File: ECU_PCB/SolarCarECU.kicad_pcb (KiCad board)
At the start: 4 copper layers, 160 x 100 mm, 121 parts, among them J1 Screw_Terminal_01x02, J2 USB_B_Micro, J3 Screw_Terminal_01x05, J4 Screw_Terminal_01x08, J5 Screw_Terminal_01x08, J6 Screw_Terminal_01x14, J7 Screw_Terminal_01x14, Q1 QM6015D, Q2 PZT2222A, Q3 QM6015D, Q4 QM6015D, Q5 QM6015D, Q6 QM6015D, U1 Teensy3.6, U10 LM324A, U2 EL7202CN, U3 EL7202CN, U4 L7805, U5 MCP2562-E-P, U6 MCP2562-E-P, U7 4504, U8 4504, U9 4504

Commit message: PCB prototype finished, documention added
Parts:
- added BT1: Battery_Cell, Battery:BatteryHolder_Keystone_1060_1x2032, F.Cu at (141.2, 65.5)
- added R52: 1k, Resistor_SMD:R_0603_1608Metric, F.Cu at (222.8, 96.3)
- added R53: 1k, Resistor_SMD:R_0603_1608Metric, F.Cu at (222.8, 98.0)
- added R54: 47, Resistor_SMD:R_0603_1608Metric, F.Cu at (237.5, 118.1)
- added R55: 47, Resistor_SMD:R_0603_1608Metric, F.Cu at (237.5, 115.6)
- added R56: 47, Resistor_SMD:R_0603_1608Metric, F.Cu at (237.5, 113.0)
- added R57: 47, Resistor_SMD:R_0603_1608Metric, F.Cu at (237.5, 110.5)
- J2: value USB_B_Micro -> USB_B; footprint SamacSys_Parts:USBRBSSOTH -> Connector_USB:USB_B_OST_USB-B1HSxx_Horizontal
- R42, R5: value 0 -> 47
- R43: footprint Resistor_SMD:R_0603_1608Metric -> Resistor_SMD:R_1206_3216Metric
- moved R42 90.2 mm to (237.5, 120.7)
- moved R5 38.1 mm to (237.5, 123.2)
- moved R43 35.8 mm to (114.6, 133.9), turned to 90 degrees
- moved R46 32.3 mm to (95.2, 119.3)
- moved R47 32.3 mm to (98.4, 119.3)
- moved C19 12.9 mm to (225.9, 60.5), turned to 0 degrees
- moved R44 10.2 mm to (96.0, 94.6)
- moved R45 10.2 mm to (99.2, 94.6)
- moved C15 6.86 mm to (225.9, 50.3), turned to 180 degrees
- moved R11 5.72 mm to (232.4, 136.9)
- moved R9 5.61 mm to (231.9, 121.2)
- moved C11 4.58 mm to (219.6, 136.3)
- moved C12 4.58 mm to (219.5, 124.7)
- moved R1 4.58 mm to (218.3, 131.2)
- moved R2 4.58 mm to (218.3, 138.8)
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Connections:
- net Net-(U1-Pad23) renamed /UART_4_RX
- net Net-(U1-Pad24) renamed /UART_4_TX
- J2 pad 4: Net-(J2-Pad4) -> GND
- J4 pad 2: /MOTOR_L_THROTTLE -> /MOTOR_R_THROTTLE
- J4 pad 3: /MOTOR_L_REGEN -> /MOTOR_R_METER
- J4 pad 4: /MOTOR_L_FWD_EN -> /MOTOR_R_REGEN_EN
- J4 pad 5: /MOTOR_L_REV_EN -> /MOTOR_R_ECO_EN
- J4 pad 6: /MOTOR_L_METER -> /MOTOR_R_FWD_EN
- J4 pad 7: /MOTOR_R_METER -> /MOTOR_R_REV_EN
- J5 pad 1: /MOTOR_R_ECO_EN -> /MOTOR_L_REGEN
- J5 pad 2: /MOTOR_R_REGEN_EN -> /MOTOR_L_THROTTLE
- J5 pad 3: /MOTOR_R_FWD_EN -> /MOTOR_L_METER
- J5 pad 6: /MOTOR_R_REV_EN -> /MOTOR_L_FWD_EN
- J5 pad 7: /MOTOR_R_THROTTLE -> /MOTOR_L_REV_EN
- J7 pad 1: +12V -> +5V
- J7 pad 10: /CS_0 -> Net-(J7-Pad10)
- J7 pad 11: /MISO_0 -> Net-(J7-Pad11)
- J7 pad 12: /MOSI_0 -> Net-(J7-Pad12)
- J7 pad 13: /SCK_0 -> Net-(J7-Pad13)
- J7 pad 6: +5V -> /SCL_0
- J7 pad 7: /UART_RX -> /SDA_0
- J7 pad 8: /UART_TX -> Net-(J7-Pad8)
- J7 pad 9: GND -> Net-(J7-Pad9)
- R42 pad 1: +12V -> Net-(J7-Pad9)
- R42 pad 2: Net-(C1-Pad1) -> /UART_1_TX
- R5 pad 1: Net-(J2-Pad4) -> Net-(J7-Pad8)
- R5 pad 2: /USB_MASTER-SLAVE_SEL -> /UART_1_RX
- U1 pad 10: Net-(U1-Pad10) -> /UART_3_TX
- U1 pad 76: Net-(U1-Pad76) -> /UART_6_RX
- U1 pad 77: Net-(U1-Pad77) -> /UART_6_TX
- U1 pad 84: /LV_HEADLIGHTS -> /LV_HORN
- U1 pad 85: /LV_HORN -> /LV_HEADLIGHTS
- U1 pad 9: Net-(U1-Pad9) -> /UART_3_RX
- U8 pad 10: /MOTOR_R_FWD_EN -> /MOTOR_L_REGEN_EN
- U8 pad 11: /LV_MOTOR_R_REGEN_EN -> GND
- U8 pad 12: /MOTOR_R_REGEN_EN -> Net-(U8-Pad12)
- U8 pad 14: /LV_MOTOR_R_ECO_EN -> GND
- U8 pad 15: /MOTOR_R_ECO_EN -> Net-(U8-Pad15)
- U8 pad 2: /MOTOR_L_REGEN_EN -> /MOTOR_L_REV_EN
- U8 pad 3: /LV_MOTOR_L_REGEN_EN -> /LV_MOTOR_L_REV_EN
- U8 pad 4: /MOTOR_L_ECO_EN -> /MOTOR_L_FWD_EN
- U8 pad 5: /LV_MOTOR_L_ECO_EN -> /LV_MOTOR_L_FWD_EN
- U8 pad 6: /MOTOR_R_REV_EN -> /MOTOR_L_ECO_EN
- U8 pad 7: /LV_MOTOR_R_REV_EN -> /LV_MOTOR_L_ECO_EN
- U8 pad 9: /LV_MOTOR_R_FWD_EN -> /LV_MOTOR_L_REGEN_EN
- U9 pad 10: /HAZARD_LED -> /MOTOR_R_REGEN_EN
- U9 pad 11: /LV_MOTOR_L_REV_EN -> /LV_MOTOR_R_ECO_EN
- U9 pad 12: /MOTOR_L_REV_EN -> /MOTOR_R_ECO_EN
- U9 pad 14: /LV_MOTOR_L_FWD_EN -> GND
- U9 pad 15: /MOTOR_L_FWD_EN -> Net-(U9-Pad15)
- U9 pad 2: Net-(U9-Pad2) -> /HAZARD_LED
- U9 pad 3: GND -> /LV_HAZARD_LED
- U9 pad 4: Net-(U9-Pad4) -> /MOTOR_R_REV_EN
- U9 pad 5: GND -> /LV_MOTOR_R_REV_EN
- U9 pad 6: Net-(U9-Pad6) -> /MOTOR_R_FWD_EN
- U9 pad 7: GND -> /LV_MOTOR_R_FWD_EN
- U9 pad 9: /LV_HAZARD_LED -> /LV_MOTOR_R_REGEN_EN
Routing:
- net +12V: track 24.5 -> 411.4 mm, vias 2 -> 12
- net +5V: track 41.4 -> 287.3 mm, vias 1 -> 4
- net /HAZARD_LED: track 0.00 -> 168.2 mm, vias 0 -> 2
- net GNDA: track 323.4 -> 207.6 mm, vias 17 -> 16
- net /LV_SEL_CTRL: track 0.00 -> 96.0 mm, vias 0 -> 1
- net /LV_UP_CTRL: track 0.00 -> 93.0 mm, vias 0 -> 1
- net /LV_GEARSHIFT_CTRL: track 3.02 -> 94.9 mm, vias 0 -> 1
- net /LV_THROTTLE_CTRL: track 3.02 -> 94.5 mm, vias 0 -> 1
- net /LV_TURNSIG_CTRL: track 3.02 -> 94.5 mm, vias 0 -> 1
- net /UART_6_RX: track 0.00 -> 90.1 mm, vias 0 -> 1
- net /UART_6_TX: track 0.00 -> 87.6 mm, vias 0 -> 1
- net /LV_DOWN_CTRL: track 0.00 -> 86.9 mm, vias 0 -> 1
- net /LV_BLINKERS: track 0.00 -> 85.3 mm, vias 0 -> 1
- net /LV_HAZARD_CTRL: track 0.00 -> 80.0 mm, vias 0 -> 1
- net /LV_HAZARD_LED: track 0.00 -> 79.8 mm
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- added copper zone on F.Cu, net +12V

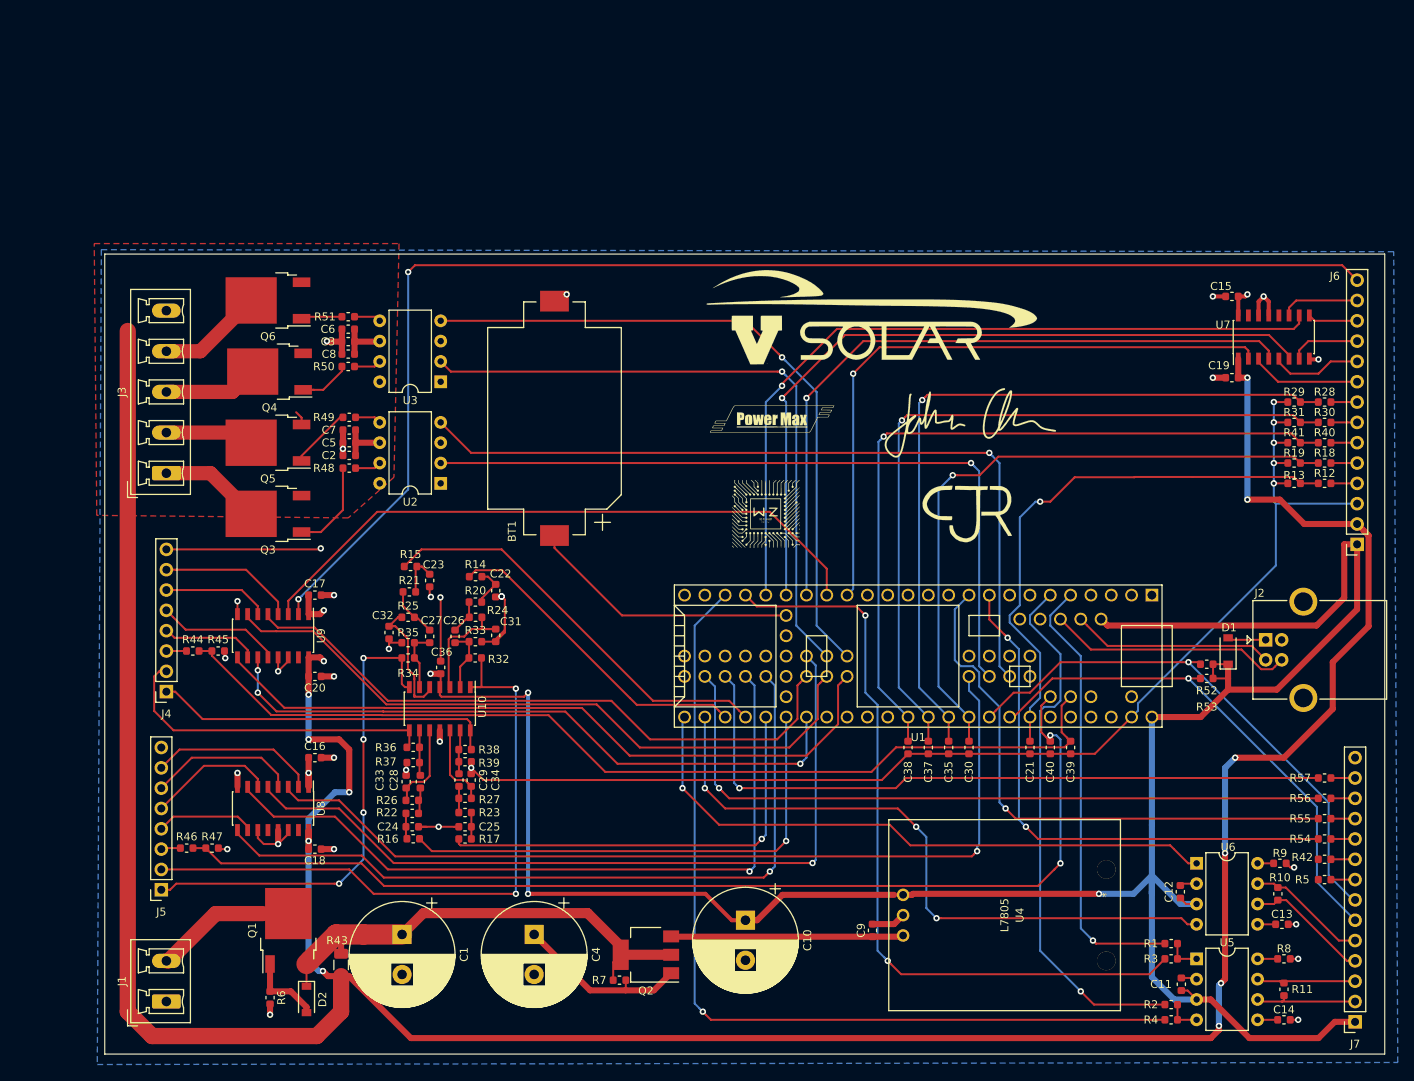
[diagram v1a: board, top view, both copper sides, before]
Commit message: fixed UART_1_* pins, added LV_KILL_SENSE, added *STEER_CTRL*
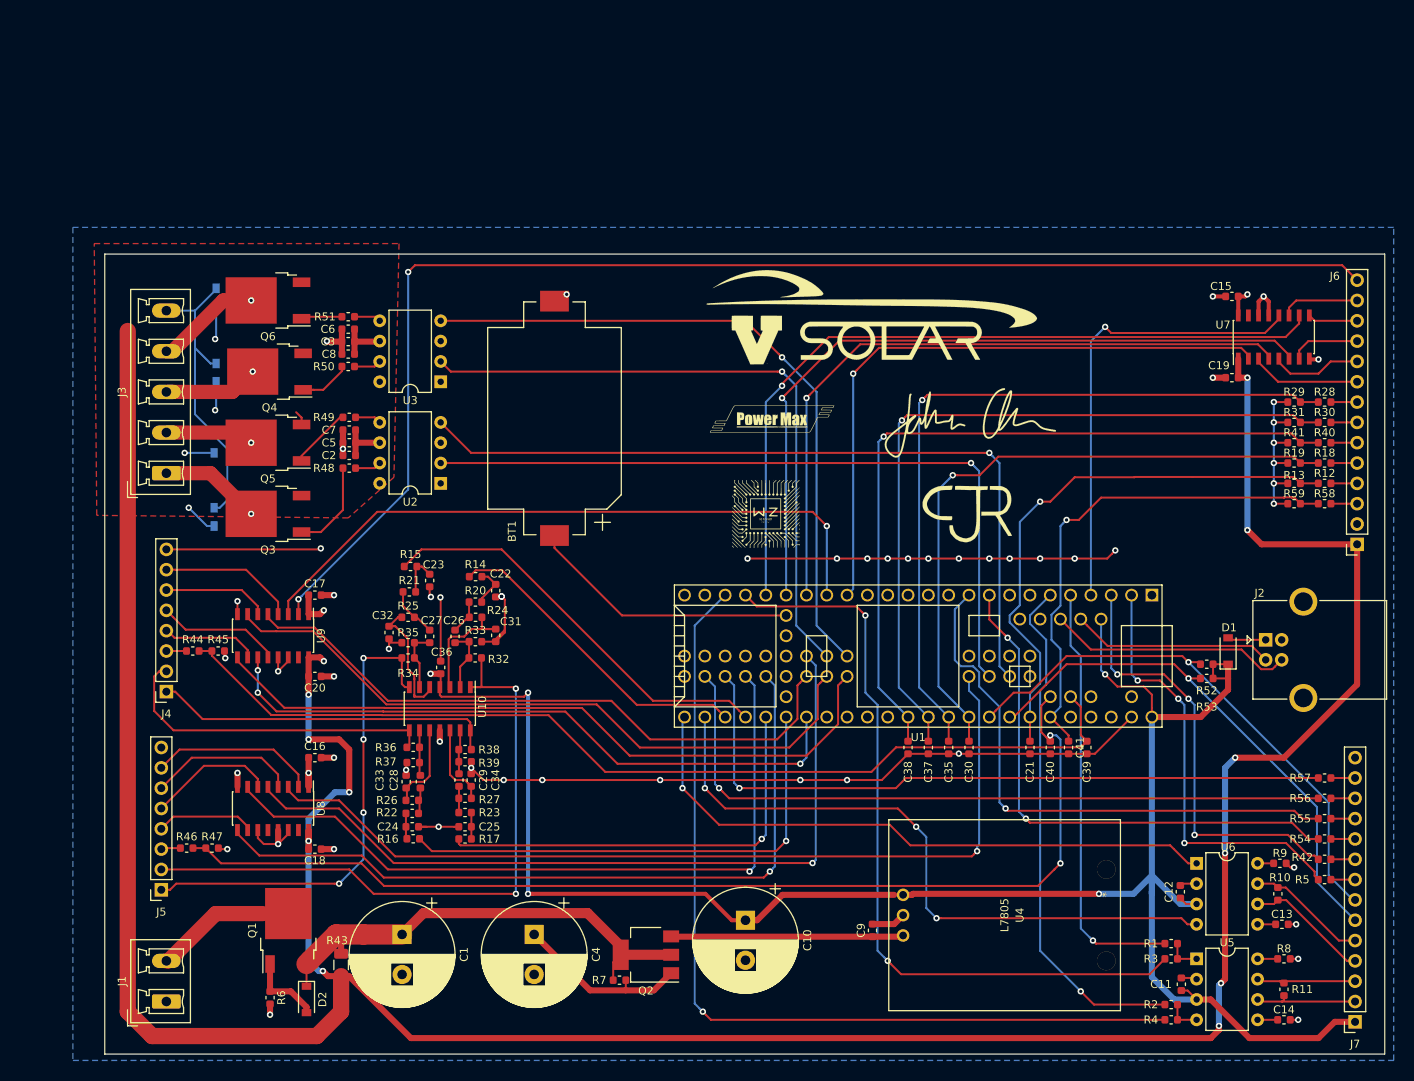
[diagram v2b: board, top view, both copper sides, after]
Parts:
- added C41: C, Capacitor_SMD:C_0603_1608Metric, F.Cu at (205.5, 106.7)
- added D10: D, Diode_SMD:D_SOD-123, B.Cu at (100.6, 49.3)
- added D3: D, Diode_SMD:D_SOD-123, B.Cu at (100.3, 79.0)
- added D4: D, Diode_SMD:D_SOD-123, B.Cu at (100.3, 76.7)
- added D5: D, Diode_SMD:D_SOD-123, B.Cu at (100.6, 61.0)
- added D6: D, Diode_SMD:D_SOD-123, B.Cu at (100.6, 58.7)
- added D7: D, Diode_SMD:D_SOD-123, B.Cu at (100.3, 69.8)
- added D8: D, Diode_SMD:D_SOD-123, B.Cu at (100.3, 67.6)
- added D9: D, Diode_SMD:D_SOD-123, B.Cu at (100.6, 51.8)
- added R58: R, Resistor_SMD:R_0603_1608Metric, F.Cu at (237.5, 76.2)
- added R59: R, Resistor_SMD:R_0603_1608Metric, F.Cu at (233.7, 76.2)
- moved C39 2.03 mm to (207.8, 106.7)
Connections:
- J6 pad 1: +5V -> +12V
- J6 pad 2: +12V -> GNDA
- J6 pad 3: GNDA -> /STEER_CTRL
- U1 pad 2: /UART_RX -> /UART_1_RX
- U1 pad 3: /UART_TX -> /UART_1_TX
- U1 pad 4: Net-(U1-Pad4) -> /LV_KILL_SENSE
- U1 pad 48: Net-(U1-Pad48) -> /LV_STEER_CTRL
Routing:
- net /LV_STEER_CTRL: track 0.00 -> 63.4 mm, vias 0 -> 1
- net /LV_KILL_SENSE: track 0.00 -> 57.5 mm, vias 0 -> 1
- net /UART_1_TX: track 0.00 -> 54.4 mm, vias 0 -> 3
- net /UART_1_RX: track 0.00 -> 54.3 mm, vias 0 -> 3
- net +5V: track 287.3 -> 235.2 mm, vias 4 -> 5
- net GND: track 55.4 -> 93.8 mm
- net +12V: track 411.4 -> 426.2 mm, vias 12 -> 16
- net GNDA: track 207.6 -> 211.5 mm, vias 16 -> 35
- net /HORN: track 12.7 -> 16.4 mm, vias 0 -> 1
- net /HEADLIGHTS: track 11.1 -> 14.7 mm, vias 0 -> 1
- net /BRAKELIGHTS: track 11.8 -> 15.3 mm, vias 0 -> 1
- net /BLINKERS: track 13.2 -> 16.7 mm, vias 0 -> 1
- net /STEER_CTRL: track 0.00 -> 3.28 mm
- net /LV_HAZARD_LED: track 79.8 -> 83.0 mm, vias 0 -> 1
- net Net-(R2-Pad2): track 67.3 -> 65.0 mm
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
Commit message: reworked PCB and fixed all issues brought up
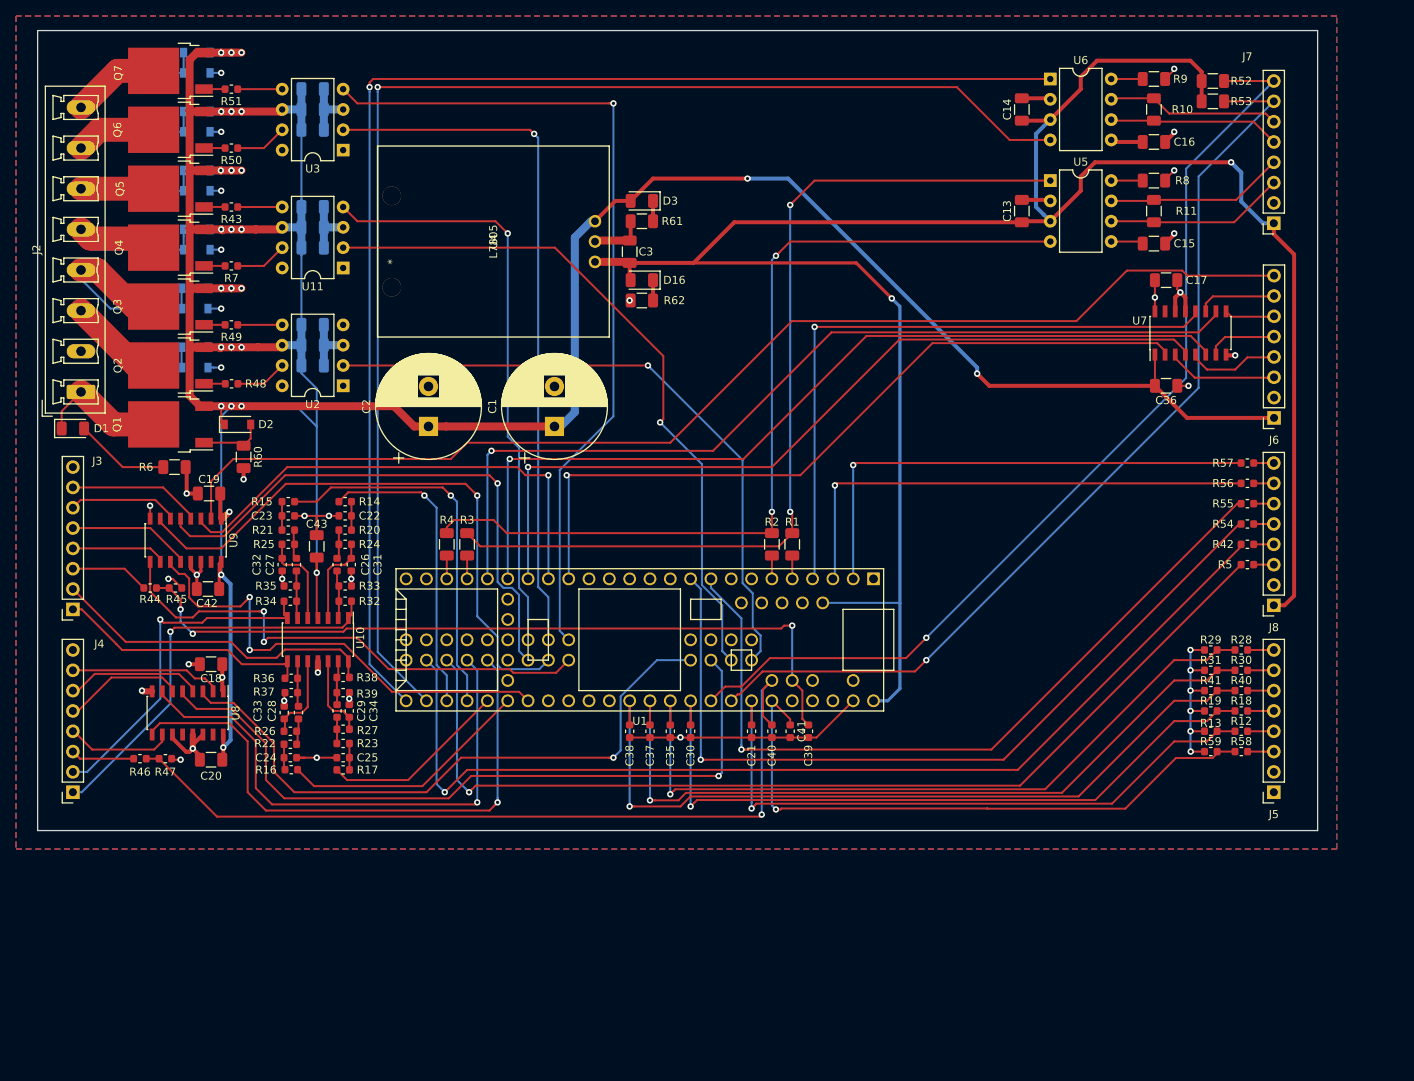
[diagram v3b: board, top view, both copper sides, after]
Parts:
- removed BT1: Battery_Cell, Battery:BatteryHolder_Keystone_1060_1x2032
- removed J1: Screw_Terminal_01x02, Connector_Phoenix_MC_HighVoltage:PhoenixContact_MCV_1,5_2-G-5.08_1x02_P5.08mm_Vertical
- added C42: 4.7u, Capacitor_SMD:C_1206_3216Metric, F.Cu at (97.9, 86.9)
- added C43: 100n, Capacitor_SMD:C_1206_3216Metric, F.Cu at (111.5, 81.5)
- added D11: D, Diode_SMD:D_SOD-123, B.Cu at (96.3, 51.8)
- added D12: D, Diode_SMD:D_SOD-123, B.Cu at (96.5, 34.5)
- added D13: D, Diode_SMD:D_SOD-123, B.Cu at (96.5, 37.1)
- added D14: D, Diode_SMD:D_SOD-123, B.Cu at (96.5, 19.8)
- added D15: D, Diode_SMD:D_SOD-123, B.Cu at (96.5, 22.4)
- added D16: 599-0291, LED_SMD:LED_1206_3216Metric, F.Cu at (152.1, 48.3)
- added J8: Screw_Terminal_01x08, Connector_PinSocket_2.54mm:PinSocket_1x08_P2.54mm_Vertical, F.Cu at (231.1, 88.9)
- added Q7: QM6015D, Package_TO_SOT_SMD:TO-252-2, F.Cu at (93.2, 22.1)
- added R60: 1k, Resistor_SMD:R_1206_3216Metric, F.Cu at (102.4, 70.4)
- added R61: 1k, Resistor_SMD:R_1206_3216Metric, F.Cu at (152.1, 40.9)
- added R62: 1k, Resistor_SMD:R_1206_3216Metric, F.Cu at (152.1, 50.8)
- added U11: MCP1403, Package_DIP:DIP-8_W7.62mm, F.Cu at (114.8, 46.7)
- C10: value 10uF -> 100n; footprint Capacitor_THT:CP_Radial_D13.0mm_P5.00mm -> Capacitor_SMD:C_1206_3216Metric; moved to B.Cu
- C11: value 0.47u -> 4.7u; footprint Capacitor_SMD:C_0603_1608Metric -> Capacitor_SMD:C_1206_3216Metric; moved to B.Cu
- C12: value 0.47u -> 47u; footprint Capacitor_SMD:C_0603_1608Metric -> Capacitor_SMD:C_1206_3216Metric; moved to B.Cu
- C13, C14, C15, C16, C17: value 0.47u -> 100n; footprint Capacitor_SMD:C_0603_1608Metric -> Capacitor_SMD:C_1206_3216Metric
- C18, C19: value 4.7u -> 100n; footprint Capacitor_SMD:C_0603_1608Metric -> Capacitor_SMD:C_1206_3216Metric
- C2: value 0.47u -> 470uF; footprint Capacitor_SMD:C_0603_1608Metric -> Capacitor_THT:CP_Radial_D13.0mm_P5.00mm
- C20: footprint Capacitor_SMD:C_0603_1608Metric -> Capacitor_SMD:C_1206_3216Metric
- C21, C30, C35, C37, C38, C39, C40, C41: value C -> 1n
- C3: value 0.47u -> 10uF; footprint Capacitor_SMD:C_0603_1608Metric -> Capacitor_SMD:C_1206_3216Metric
- C36: value 0.47u -> 4.7u; footprint Capacitor_SMD:C_0603_1608Metric -> Capacitor_SMD:C_1206_3216Metric
- C4: value 470uF -> 100n; footprint Capacitor_THT:CP_Radial_D13.0mm_P5.00mm -> Capacitor_SMD:C_1206_3216Metric; moved to B.Cu
- C5: footprint Capacitor_SMD:C_0603_1608Metric -> Capacitor_SMD:C_1206_3216Metric; moved to B.Cu
- C6: value 4.7u -> 47u; footprint Capacitor_SMD:C_0603_1608Metric -> Capacitor_SMD:C_1206_3216Metric; moved to B.Cu
- C7: value 47u -> 100n; footprint Capacitor_SMD:C_0603_1608Metric -> Capacitor_SMD:C_1206_3216Metric; moved to B.Cu
- C8: value 47u -> 4.7u; footprint Capacitor_SMD:C_0603_1608Metric -> Capacitor_SMD:C_1206_3216Metric; moved to B.Cu
- C9: value 10uF -> 47u; footprint Capacitor_SMD:C_0603_1608Metric -> Capacitor_SMD:C_1206_3216Metric; moved to B.Cu
- D1: value D_Schottky -> 599-0210; footprint Diode_SMD:D_SOD-123 -> LED_SMD:LED_1206_3216Metric
- D3: value D -> 599-0230; footprint Diode_SMD:D_SOD-123 -> LED_SMD:LED_1206_3216Metric; moved to F.Cu
- G*** (x5): moved to B.Cu
- J2: value USB_B -> Screw_Terminal_01x08; footprint Connector_USB:USB_B_OST_USB-B1HSxx_Horizontal -> Connector_Phoenix_MC_HighVoltage:PhoenixContact_MCV_1,5_8-G-5.08_1x08_P5.08mm_Vertical
- J3: value Screw_Terminal_01x05 -> Screw_Terminal_01x08; footprint Connector_Phoenix_MC_HighVoltage:PhoenixContact_MCV_1,5_5-G-5.08_1x05_P5.08mm_Vertical -> Connector_PinSocket_2.54mm:PinSocket_1x08_P2.54mm_Vertical
- J6, J7: value Screw_Terminal_01x14 -> Screw_Terminal_01x08; footprint Connector_PinSocket_2.54mm:PinSocket_1x14_P2.54mm_Vertical -> Connector_PinSocket_2.54mm:PinSocket_1x08_P2.54mm_Vertical
- Q2: value PZT2222A -> QM6015D; footprint Package_TO_SOT_SMD:SOT-223 -> Package_TO_SOT_SMD:TO-252-2
- R1, R10, R11, R2, R3, R4, R52, R53, R6, R8, R9: footprint Resistor_SMD:R_0603_1608Metric -> Resistor_SMD:R_1206_3216Metric
- R12, R18, R28, R30, R40, R44, R46, R58: value R -> 1M
- R13, R19, R29, R31, R41, R45, R47, R59: value R -> 330k
- R43: value 0 -> 4.7; footprint Resistor_SMD:R_1206_3216Metric -> Resistor_SMD:R_0603_1608Metric
- R7: value 120 -> 4.7
- U2, U3: value EL7202CN -> MCP1403
- moved C11 154.1 mm to (111.0, 26.9), turned to 180 degrees
- moved J2 151.3 mm to (82.0, 62.2), turned to 90 degrees
- moved D1 147.1 mm to (81.0, 66.8), turned to 0 degrees
- moved C12 144.3 mm to (111.0, 29.5), turned to 180 degrees
- moved J5 139.6 mm to (231.1, 112.3)
- moved C16 130.1 mm to (216.2, 31.0)
- moved C19 128.7 mm to (98.0, 74.9), turned to 180 degrees
- moved U4 119.3 mm to (120.9, 46.0), turned to 90 degrees
- moved C14 118.4 mm to (199.6, 26.9), turned to 90 degrees
- moved C10 117.1 mm to (111.0, 24.4), turned to 180 degrees
- moved C17 113.5 mm to (217.7, 48.3)
- moved C9 110.4 mm to (111.0, 44.2), turned to 180 degrees
- moved R4 108.3 mm to (127.8, 81.3), turned to 270 degrees
- moved R3 102.1 mm to (130.3, 81.3), turned to 270 degrees
- moved R7 101.6 mm to (100.8, 46.5)
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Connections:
- net /LV_BLINKERS renamed /LV_LEFT_BLINKERS
- C1 pad 1: Net-(C1-Pad1) -> +12V
- C10 pad 1: +5V -> GND
- C10 pad 2: GND -> +12V
- C11 pad 1: +5V -> GND
- C11 pad 2: GND -> +12V
- C12 pad 1: +5V -> GND
- C12 pad 2: GND -> +12V
- C13 pad 1: +3V3 -> +5V
- C14 pad 1: +3V3 -> +5V
- C18 pad 1: GND -> +3V3
- C18 pad 2: +12V -> GND
- C19 pad 1: GND -> +3V3
- C19 pad 2: +12V -> GND
- C2 pad 1: GND -> +12V
- C2 pad 2: +12V -> GND
- C3 pad 1: GND -> +5V
- C3 pad 2: +12V -> GND
- C36 pad 1: GNDA -> GND
- C36 pad 2: +5V -> +12V
- C4 pad 1: Net-(C4-Pad1) -> GND
- C4 pad 2: GND -> +12V
- C9 pad 1: Net-(C9-Pad1) -> GND
- C9 pad 2: GND -> +12V
- D1 pad 1: +5V -> +VDC
- D10 pad 1: /BLINKERS -> +12V
- D10 pad 2: GND -> /STROBE
- D2 pad 1: Net-(C1-Pad1) -> +12V
- D3 pad 1: +12V -> Net-(D3-Pad1)
- D3 pad 2: /HORN -> +12V
- D4 pad 1: /HORN -> +12V
- D4 pad 2: GND -> /HORN
- D5 pad 1: +12V -> /HORN
- D5 pad 2: /BRAKELIGHTS -> GND
- D6 pad 1: /BRAKELIGHTS -> +12V
- D6 pad 2: GND -> /BRAKELIGHTS
- D7 pad 1: +12V -> /BRAKELIGHTS
- D7 pad 2: /HEADLIGHTS -> GND
- D8 pad 1: /HEADLIGHTS -> +12V
- D8 pad 2: GND -> /RIGHT_BLINKERS
- D9 pad 1: +12V -> /RIGHT_BLINKERS
- D9 pad 2: /BLINKERS -> GND
- J2 pad 1: Net-(D1-Pad2) -> +VDC
- J2 pad 2: /USB_D- -> GND
- J2 pad 3: /USB_D+ -> /HORN
- J2 pad 4: GND -> /STROBE
- J2 pad 5: GND -> /BRAKELIGHTS
- J3 pad 1: /HORN -> /MOTOR_R_THROTTLE
- J3 pad 2: /HEADLIGHTS -> /MOTOR_R_REGEN
- J3 pad 3: /BRAKELIGHTS -> /MOTOR_R_METER
- J3 pad 4: /BLINKERS -> /MOTOR_R_REGEN_EN
- J3 pad 5: GND -> /MOTOR_R_ECO_EN
- J4 pad 1: /MOTOR_R_REGEN -> /MOTOR_L_THROTTLE
- J4 pad 2: /MOTOR_R_THROTTLE -> /MOTOR_L_REGEN
- J4 pad 3: /MOTOR_R_METER -> /MOTOR_L_METER
- J4 pad 4: /MOTOR_R_REGEN_EN -> /MOTOR_L_REGEN_EN
- J4 pad 5: /MOTOR_R_ECO_EN -> /MOTOR_L_ECO_EN
- J4 pad 6: /MOTOR_R_FWD_EN -> /MOTOR_L_FWD_EN
- J4 pad 7: /MOTOR_R_REV_EN -> /MOTOR_L_REV_EN
- J5 pad 1: /MOTOR_L_REGEN -> +12V
- J5 pad 2: /MOTOR_L_THROTTLE -> GNDA
- J5 pad 3: /MOTOR_L_METER -> /STEER_CTRL
- J5 pad 4: /MOTOR_L_REGEN_EN -> /BRAKE_CTRL
- J5 pad 5: /MOTOR_L_ECO_EN -> /REGEN_CTRL
- J5 pad 6: /MOTOR_L_FWD_EN -> /GEARSHIFT_CTRL
- J5 pad 7: /MOTOR_L_REV_EN -> /TURNSIG_CTRL
- J5 pad 8: GNDA -> /THROTTLE_CTRL
- J6 pad 3: /STEER_CTRL -> /HAZARD_CTRL
- J6 pad 4: /BRAKE_CTRL -> /DOWN_CTRL
- J6 pad 5: /REGEN_CTRL -> /UP_CTRL
- J6 pad 6: /GEARSHIFT_CTRL -> /SEL_CTRL
- J6 pad 7: /TURNSIG_CTRL -> /KILL_SENSE
- J6 pad 8: /THROTTLE_CTRL -> /HAZARD_LED
- J7 pad 2: /CAN0_L -> GND
- J7 pad 3: /CAN0_H -> /CAN0_L
- J7 pad 4: /CAN1_L -> /CAN0_H
- J7 pad 5: /CAN1_H -> /CAN1_L
- J7 pad 6: /SCL_0 -> /CAN1_H
- J7 pad 7: /SDA_0 -> /SCL_0
- J7 pad 8: Net-(J7-Pad8) -> /SDA_0
- Q1 pad 2: Net-(J1-Pad2) -> +VDC
- Q1 pad 3: Net-(C1-Pad1) -> +12V
- Q2 pad 1: Net-(C4-Pad1) -> Net-(Q2-Pad1)
- Q2 pad 2: Net-(C1-Pad1) -> /HORN
- Q2 pad 3: Net-(C9-Pad1) -> +12V
- Q3 pad 2: /HORN -> /STROBE
- Q6 pad 2: /BLINKERS -> /RIGHT_BLINKERS
- R42 pad 1: Net-(J7-Pad9) -> Net-(J8-Pad4)
- R42 pad 2: /UART_1_TX -> /UART_6_RX
- R43 pad 1: +12V -> Net-(Q5-Pad1)
- R43 pad 2: Net-(C1-Pad1) -> Net-(R43-Pad2)
- R48 pad 1: Net-(Q3-Pad1) -> Net-(Q2-Pad1)
- R49 pad 1: Net-(Q5-Pad1) -> Net-(Q3-Pad1)
- R5 pad 1: Net-(J7-Pad8) -> Net-(J8-Pad3)
- R5 pad 2: /UART_1_RX -> /UART_6_TX
- R50 pad 1: Net-(Q4-Pad1) -> Net-(Q6-Pad1)
- R51 pad 1: Net-(Q6-Pad1) -> Net-(Q7-Pad1)
- R54 pad 1: Net-(J7-Pad10) -> Net-(J8-Pad5)
- R54 pad 2: /UART_3_RX -> /UART_3_TX
- R55 pad 1: Net-(J7-Pad11) -> Net-(J8-Pad6)
- R55 pad 2: /UART_3_TX -> /UART_3_RX
- R56 pad 1: Net-(J7-Pad12) -> Net-(J8-Pad7)
- R56 pad 2: /UART_6_RX -> /UART_1_TX
- R57 pad 1: Net-(J7-Pad13) -> Net-(J8-Pad8)
- R57 pad 2: /UART_6_TX -> /UART_1_RX
- R6 pad 1: Net-(D2-Pad2) -> Net-(D1-Pad2)
- R7 pad 1: Net-(C1-Pad1) -> Net-(Q4-Pad1)
- R7 pad 2: Net-(C4-Pad1) -> Net-(R7-Pad2)
- U1 pad 68: /LV_BRAKELIGHTS -> /LV_RIGHT_BLINKERS
- U1 pad 69: /LV_MOTOR_L_FWD_EN -> /LV_HEADLIGHTS
- U1 pad 84: /LV_HORN -> /LV_MOTOR_L_FWD_EN
- U1 pad 85: /LV_HEADLIGHTS -> /LV_BRAKELIGHTS
- U1 pad 86: /USB_MASTER-SLAVE_SEL -> /LV_HORN
- U10 pad 4: +5V -> +12V
- U2 pad 4: /LV_HEADLIGHTS -> /LV_STROBE
- U3 pad 2: /LV_BRAKELIGHTS -> /LV_RIGHT_BLINKERS
- U4 pad 1: Net-(C9-Pad1) -> +12V
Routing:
- net GNDA: track 211.5 -> 78.0 mm, vias 35 -> 16
- net /CAN0_TX: track 4.29 -> 116.9 mm, vias 0 -> 2
- net Net-(R4-Pad2): track 112.2 -> 2.92 mm, vias 1 -> 0
- net /CAN0_RX: track 4.29 -> 112.3 mm, vias 0 -> 2
- net Net-(R3-Pad2): track 96.5 -> 2.92 mm, vias 2 -> 0
- net /LV_RIGHT_BLINKERS: track 0.00 -> 88.1 mm, vias 0 -> 1
- net /CAN1_TX: track 77.1 -> 164.4 mm
- net /CAN1_RX: track 82.6 -> 166.0 mm, vias 3 -> 1
- net Net-(R2-Pad2): track 65.0 -> 2.92 mm, vias 1 -> 0
- net Net-(C1-Pad1): track 61.2 -> 0.00 mm
- net /SDA_0: track 68.5 -> 124.0 mm
- net /SCL_0: track 66.2 -> 120.5 mm
- net Net-(R1-Pad2): track 53.6 -> 2.92 mm, vias 1 -> 0
- net +5V: track 235.2 -> 283.6 mm, vias 5 -> 2
- net /UART_6_RX: track 90.1 -> 130.0 mm
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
